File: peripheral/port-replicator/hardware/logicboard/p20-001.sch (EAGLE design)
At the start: 8 parts, among them J1 DIN5, J2 DIN5, J3 DIN5

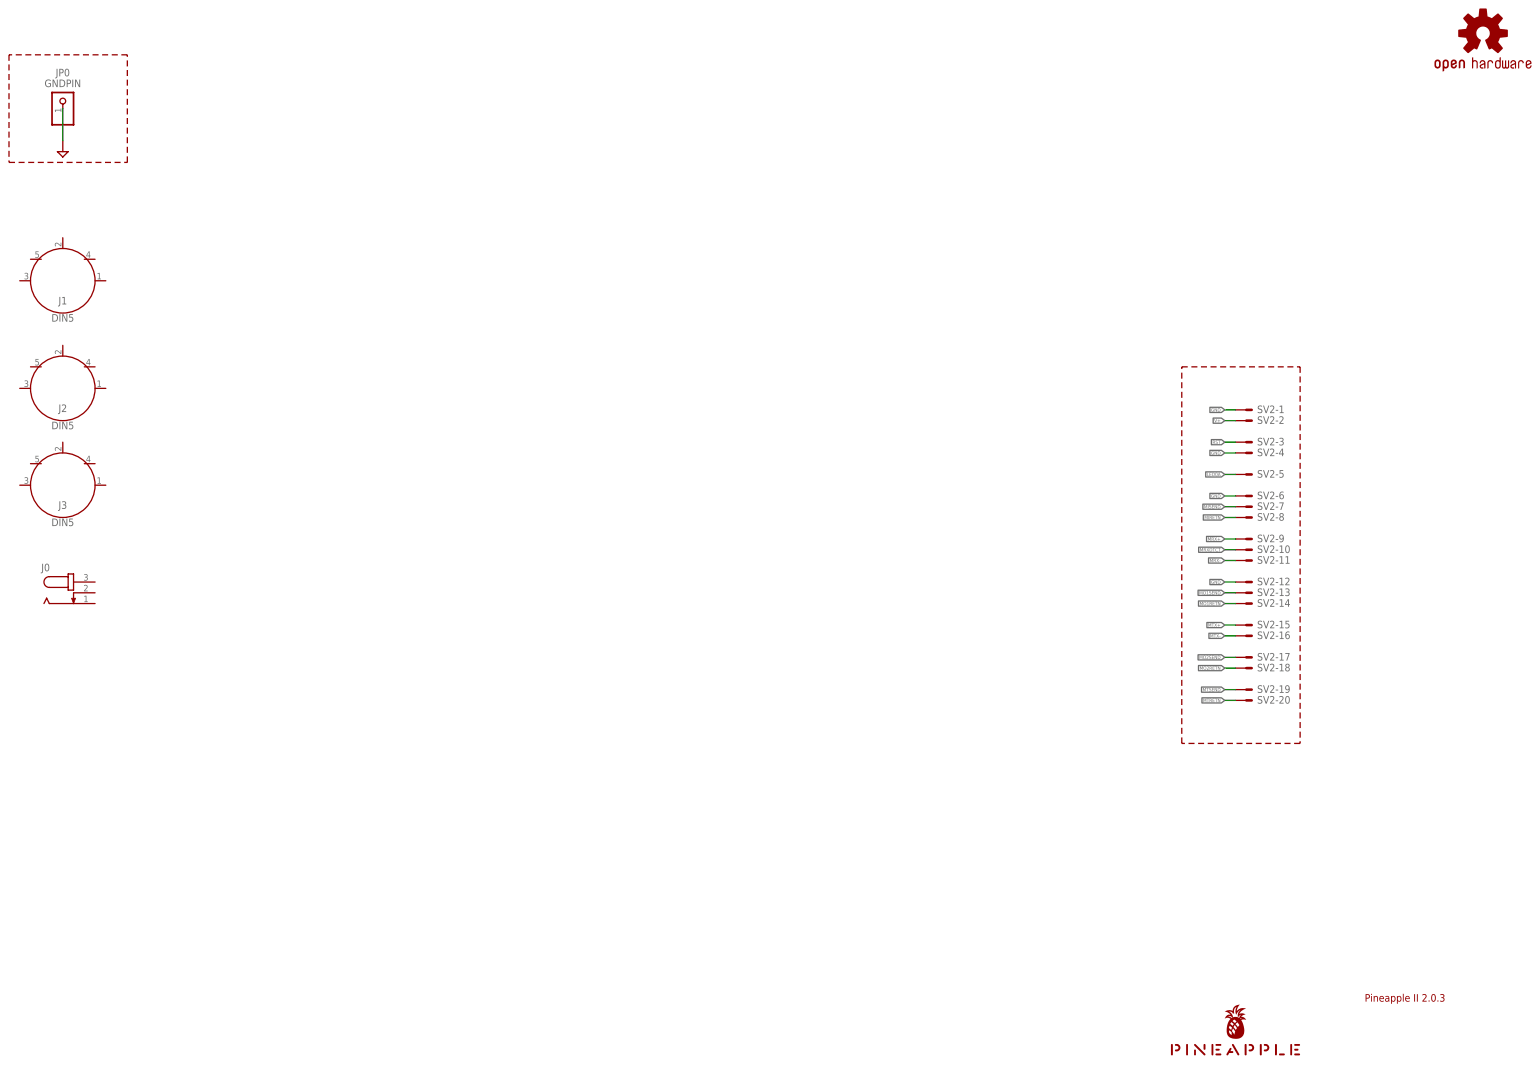
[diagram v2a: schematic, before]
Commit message: The first artwork for MIDI Port Replicator.
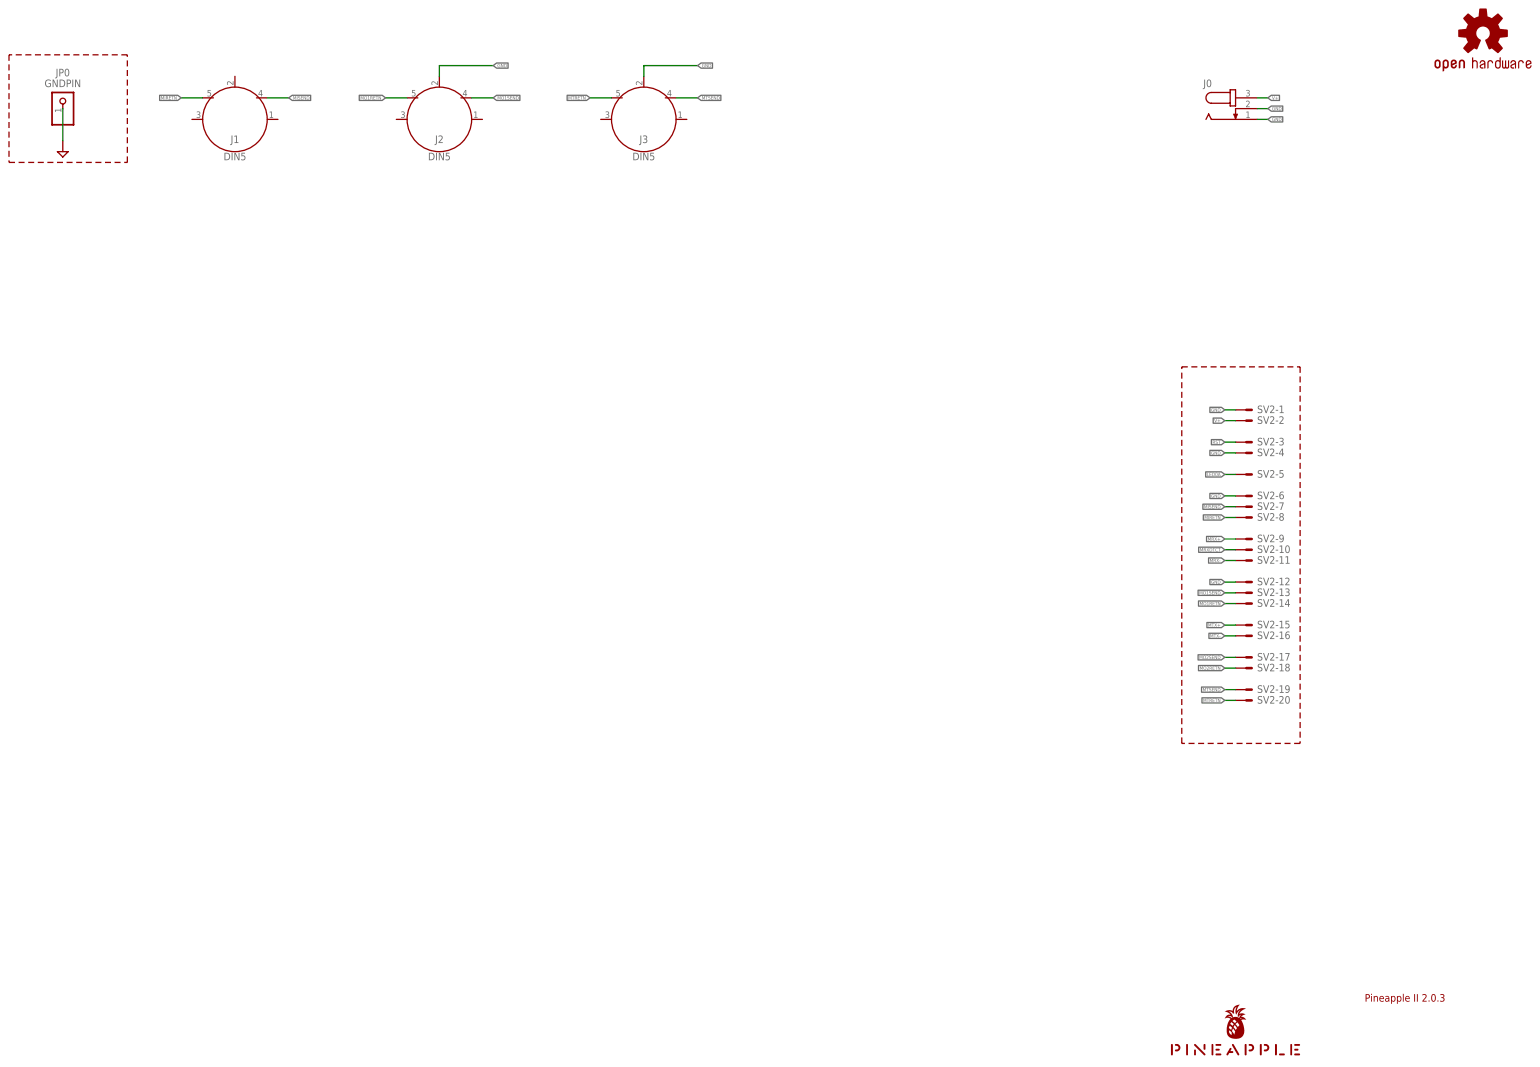
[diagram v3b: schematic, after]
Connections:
- net GND: now also J0.1, J0.2, J2.2, J3.2
- net MIRETN: now also J1.5
- net MISEND: now also J1.4
- net MO1RETN: now also J2.5
- net MO1SEND: now also J2.4
- net MTRETN: now also J3.5
- net MTSEND: now also J3.4
- net V+: now also J0.3
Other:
- moved on the sheet: J0, J1, J2, J3
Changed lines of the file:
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@@
 </instance>
 <instance part="SUPPLY33" gate="GND" x="35.56" y="220.98" smashed="yes"/>
-<instance part="J1" gate="G$1" x="35.56" y="190.5" smashed="yes">
-<attribute name="NAME" x="35.56" y="184.912" size="1.778" layer="95" font="vector" align="bottom-center"/>
-<attribute name="VALUE" x="35.56" y="182.626" size="1.778" layer="96" font="vector" align="top-center"/>
-</instance>
-<instance part="J2" gate="G$1" x="35.56" y="165.1" smashed="yes">
-<attribute name="NAME" x="35.56" y="159.512" size="1.778" layer="95" font="vector" align="bottom-center"/>
-<attribute name="VALUE" x="35.56" y="157.226" size="1.778" layer="96" font="vector" align="top-center"/>
-</instance>
-<instance part="J3" gate="G$1" x="35.56" y="142.24" smashed="yes">
-<attribute name="NAME" x="35.56" y="136.652" size="1.778" layer="95" font="vector" align="bottom-center"/>
-<attribute name="VALUE" x="35.56" y="134.366" size="1.778" layer="96" font="vector" align="top-center"/>
-</instance>
-<instance part="J0" gate="G$1" x="38.1" y="116.84" smashed="yes">
-<attribute name="NAME" x="30.48" y="121.92" size="1.778" layer="95"/>
-<attribute name="VALUE" x="30.48" y="111.76" size="1.778" layer="96"/>
+<instance part="J1" gate="G$1" x="76.2" y="228.6" smashed="yes">
+<attribute name="NAME" x="76.2" y="223.012" size="1.778" layer="95" font="vector" align="bottom-center"/>
+<attribute name="VALUE" x="76.2" y="220.726" size="1.778" layer="96" font="vector" align="top-center"/>
+</instance>
+<instance part="J2" gate="G$1" x="124.46" y="228.6" smashed="yes">
+<attribute name="NAME" x="124.46" y="223.012" size="1.778" layer="95" font="vector" align="bottom-center"/>
+<attribute name="VALUE" x="124.46" y="220.726" size="1.778" layer="96" font="vector" align="top-center"/>
+</instance>
+<instance part="J3" gate="G$1" x="172.72" y="228.6" smashed="yes">
+<attribute name="NAME" x="172.72" y="223.012" size="1.778" layer="95" font="vector" align="bottom-center"/>
+<attribute name="VALUE" x="172.72" y="220.726" size="1.778" layer="96" font="vector" align="top-center"/>
+</instance>
+<instance part="J0" gate="G$1" x="312.42" y="231.14" smashed="yes">
+<attribute name="NAME" x="304.8" y="236.22" size="1.778" layer="95"/>
+<attribute name="VALUE" x="304.8" y="226.06" size="1.778" layer="96"/>
 </instance>
 </instances>
@@
 <label x="309.88" y="160.02" size="0.8128" layer="95" rot="MR0" xref="yes"/>
 </segment>
+<segment>
+<pinref part="J2" gate="G$1" pin="2"/>
+<wire x1="124.46" y1="238.76" x2="124.46" y2="241.3" width="0.1524" layer="91"/>
+<wire x1="124.46" y1="241.3" x2="137.16" y2="241.3" width="0.1524" layer="91"/>
+<label x="137.16" y="241.3" size="0.8128" layer="95" xref="yes"/>
+</segment>
+<segment>
+<pinref part="J3" gate="G$1" pin="2"/>
+<wire x1="172.72" y1="238.76" x2="172.72" y2="241.3" width="0.1524" layer="91"/>
+<wire x1="172.72" y1="241.3" x2="185.42" y2="241.3" width="0.1524" layer="91"/>
+<label x="185.42" y="241.3" size="0.8128" layer="95" xref="yes"/>
+</segment>
+<segment>
+<pinref part="J0" gate="G$1" pin="2"/>
+<wire x1="317.5" y1="231.14" x2="320.04" y2="231.14" width="0.1524" layer="91"/>
+<label x="320.04" y="231.14" size="0.8128" layer="95" xref="yes"/>
+</segment>
+<segment>
+<pinref part="J0" gate="G$1" pin="1"/>
+<wire x1="317.5" y1="228.6" x2="320.04" y2="228.6" width="0.1524" layer="91"/>
+<label x="320.04" y="228.6" size="0.8128" layer="95" xref="yes"/>
+</segment>
 </net>
 <net name="MTX+" class="0">
@@
 <label x="309.88" y="137.16" size="0.8128" layer="95" rot="MR0" xref="yes"/>
 </segment>
+<segment>
+<pinref part="J1" gate="G$1" pin="4"/>
+<wire x1="83.82" y1="233.68" x2="88.9" y2="233.68" width="0.1524" layer="91"/>
+<label x="88.9" y="233.68" size="0.8128" layer="95" xref="yes"/>
+</segment>
 </net>
 <net name="MIRETN" class="0">
@@
 <label x="309.88" y="134.62" size="0.8128" layer="95" rot="MR0" xref="yes"/>
 </segment>
+<segment>
+<pinref part="J1" gate="G$1" pin="5"/>
+<wire x1="68.58" y1="233.68" x2="63.5" y2="233.68" width="0.1524" layer="91"/>
+<label x="63.5" y="233.68" size="0.8128" layer="95" rot="R180" xref="yes"/>
+</segment>
 </net>
 <net name="MTRETN" class="0">
@@
 <label x="309.88" y="91.44" size="0.8128" layer="95" rot="MR0" xref="yes"/>
 </segment>
+<segment>
+<pinref part="J3" gate="G$1" pin="5"/>
+<wire x1="165.1" y1="233.68" x2="160.02" y2="233.68" width="0.1524" layer="91"/>
+<label x="160.02" y="233.68" size="0.8128" layer="95" rot="R180" xref="yes"/>
+</segment>
 </net>
 <net name="MTSEND" class="0">
@@
 <label x="309.88" y="93.98" size="0.8128" layer="95" rot="MR0" xref="yes"/>
 </segment>
+<segment>
+<pinref part="J3" gate="G$1" pin="4"/>
+<wire x1="180.34" y1="233.68" x2="185.42" y2="233.68" width="0.1524" layer="91"/>
+<label x="185.42" y="233.68" size="0.8128" layer="95" xref="yes"/>
+</segment>
 </net>
 <net name="MO1RETN" class="0">
@@
 <label x="309.88" y="114.3" size="0.8128" layer="95" rot="MR0" xref="yes"/>
 </segment>
+<segment>
+<pinref part="J2" gate="G$1" pin="5"/>
+<wire x1="116.84" y1="233.68" x2="111.76" y2="233.68" width="0.1524" layer="91"/>
+<label x="111.76" y="233.68" size="0.8128" layer="95" rot="R180" xref="yes"/>
+</segment>
 </net>
 <net name="MO1SEND" class="0">
@@
 <label x="309.88" y="116.84" size="0.8128" layer="95" rot="MR0" xref="yes"/>
 </segment>
+<segment>
+<pinref part="J2" gate="G$1" pin="4"/>
+<wire x1="132.08" y1="233.68" x2="137.16" y2="233.68" width="0.1524" layer="91"/>
+<label x="137.16" y="233.68" size="0.8128" layer="95" xref="yes"/>
+</segment>
 </net>
 <net name="MO2RETN" class="0">
@@
 <label x="309.88" y="157.48" size="0.8128" layer="95" rot="MR0" xref="yes"/>
 </segment>
-</net>
+<segment>
+<pinref part="J0" gate="G$1" pin="3"/>
+<wire x1="317.5" y1="233.68" x2="320.04" y2="233.68" width="0.1524" layer="91"/>
+<label x="320.04" y="233.68" size="0.8128" layer="95" xref="yes"/>
+</segment>
+</net>

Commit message: Remake of port rep.
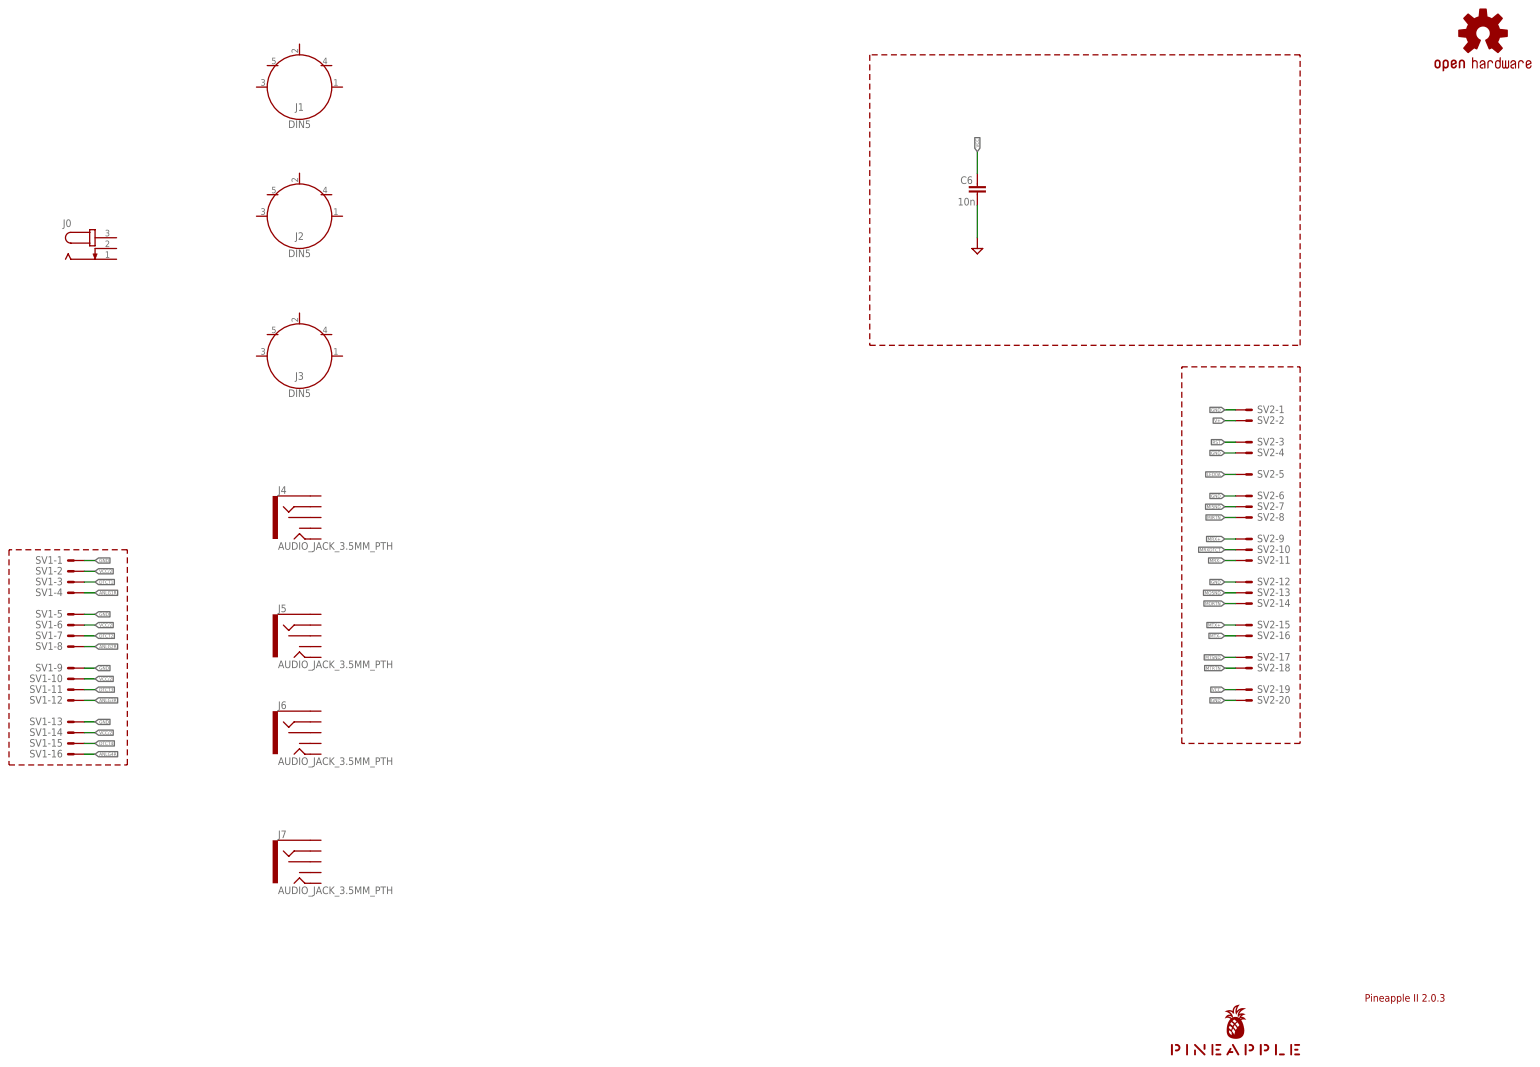
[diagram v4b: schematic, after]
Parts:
- removed JP0: GNDPIN, pinhead:PINHD-1X1
- added C6: 10n, resistor:C-EU025-024X044
- added J4, J5, J6, J7: AUDIO_JACK_3.5MM_PTH, SparkFun-Connectors:AUDIO_JACK_3.5MM_PTH
- added SV1: (no value), con-ml:ML16LE
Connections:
- net MO2RETN renamed MTRTN
- net MO2SEND renamed MTSND
- removed net MIRETN: J1.5, SV2-8.S
- removed net MISEND: J1.4, SV2-7.S
- removed net MO1RETN: J2.5, SV2-14.S
- removed net MO1SEND: J2.4, SV2-13.S
- removed net MTRETN: J3.5, SV2-20.S
- removed net MTSEND: J3.4, SV2-19.S
- new net ANLG1R: SV1-4.S
- new net ANLG2R: SV1-8.S
- new net ANLG3R: SV1-12.S
- new net ANLG4R: SV1-16.S
- new net DTCT1: SV1-3.S
- new net DTCT2: SV1-7.S
- new net DTCT3: SV1-11.S
- new net DTCT4: SV1-15.S
- new net MIRTN: SV2-8.S
- new net MISND: SV2-7.S
- new net MORTN: SV2-14.S
- new net MOSND: SV2-13.S
- new net VCC: C6.1, SV2-19.S
- new net VCC/2: SV1-10.S, SV1-14.S, SV1-2.S, SV1-6.S
- net GND: now also C6.2, SV1-1.S, SV1-13.S, SV1-5.S, SV1-9.S, SV2-20.S; no longer J0.1, J0.2, J2.2, J3.2, JP0.1
- net V+: no longer J0.3
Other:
- moved on the sheet: J0, J1, J2, J3

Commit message: Hmm...
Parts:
- removed J5, J6, J7: AUDIO_JACK_3.5MM_PTH, SparkFun-Connectors:AUDIO_JACK_3.5MM_PTH
- added J11, J12, J13: DIN5, SparkFun-Connectors:DIN5
- J1, J2, J3: value DIN5 -> AUDIO_JACK_3.5MM_PTH; device SparkFun-Connectors:DIN5 -> SparkFun-Connectors:AUDIO_JACK_3.5MM_PTH
- renumbered C6 to C1
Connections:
- net GND: now also J0.1, J0.2, J12.2, J13.2
- net MIRTN: now also J11.5
- net MISND: now also J11.4
- net MORTN: now also J13.5
- net MOSND: now also J13.4
- net MTRTN: now also J12.5
- net MTSND: now also J12.4
- net V+: now also J0.3
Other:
- moved on the sheet: J4

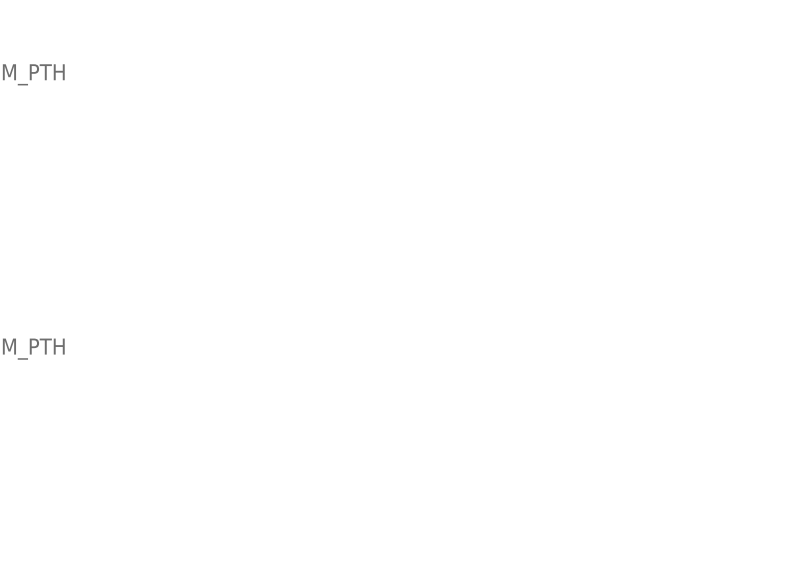
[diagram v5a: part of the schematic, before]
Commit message: Trying to implement a port replicator.
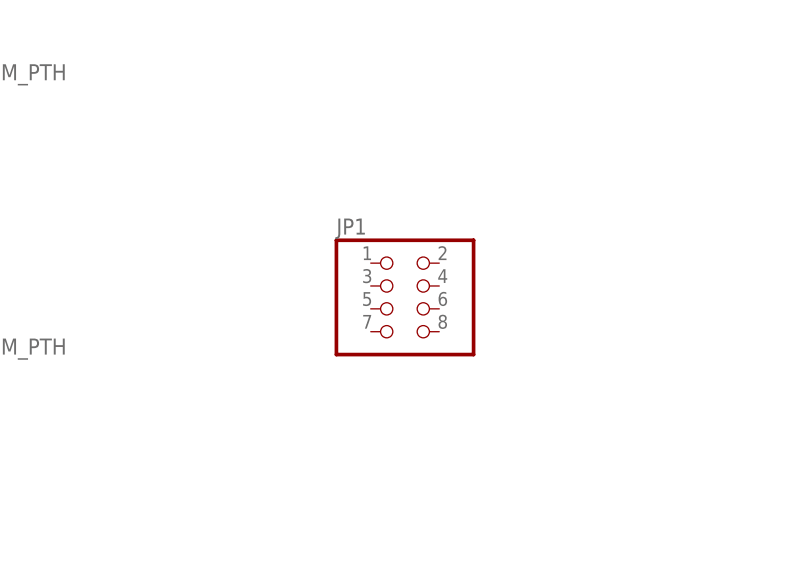
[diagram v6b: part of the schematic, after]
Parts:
- added JP1: (no value), adafruit:PINHD-2X4
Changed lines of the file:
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@@
 <part name="J3" library="SparkFun-Connectors" library_urn="urn:adsk.eagle:library:513" deviceset="AUDIO_JACK_3.5MM" device="_PTH" package3d_urn="urn:adsk.eagle:package:37997/1"/>
 <part name="J4" library="SparkFun-Connectors" library_urn="urn:adsk.eagle:library:513" deviceset="AUDIO_JACK_3.5MM" device="_PTH" package3d_urn="urn:adsk.eagle:package:37997/1"/>
+<part name="JP1" library="adafruit" library_urn="urn:adsk.eagle:library:420" deviceset="PINHD-2X4" device="" package3d_urn="urn:adsk.eagle:package:6240893/1"/>
 </parts>
 <sheets>
@@
 <attribute name="VALUE" x="86.36" y="45.72" size="1.778" layer="96" font="vector"/>
 </instance>
+<instance part="JP1" gate="A" x="149.86" y="50.8" smashed="yes">
+<attribute name="NAME" x="143.51" y="59.055" size="1.778" layer="95"/>
+<attribute name="VALUE" x="143.51" y="43.18" size="1.778" layer="96"/>
+</instance>
 </instances>

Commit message: Initial layout.
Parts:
- added IC1: 74LS07N, 74xx-us:74LS07N
- added LED1, LED2, LED3: (no value), led:LED3MM
- added R1, R2, R3: (no value), rcl:R-EU_0204/5
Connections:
- new net ANGL4R: J4.RING
- new net N$1: IC1A.O, R2.1
- new net N$2: IC1B.O, R3.1
- new net N$3: LED2.C, R2.2
- new net N$4: LED3.C, R3.2
- net ANLG1R: now also J1.RING
- net ANLG2R: now also J2.RING
- net ANLG3R: now also J3.RING
- net DTCT1: now also JP1.1
- net DTCT2: now also JP1.3
- net DTCT3: now also JP1.5
- net DTCT4: now also JP1.7
- net GND: now also IC1C.I, IC1D.I, IC1E.I, IC1F.I, J1.SLEEVE, J2.SLEEVE, J3.SLEEVE, J4.SLEEVE, JP1.2, JP1.4, JP1.6, JP1.8
- net MIRTN: now also IC1A.I
- net MOSND: now also IC1B.I
- net VCC: now also LED2.A, LED3.A
- net VCC/2: now also J1.TIP, J2.TIP, J3.TIP, J4.TIP
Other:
- moved on the sheet: JP1
